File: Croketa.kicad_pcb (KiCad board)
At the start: 2 copper layers, 17.8 x 33 mm, 23 parts, among them J1 USB_B_Micro, J2 CORTEX_DEBUGPTH, P1 Digital, P3 Analog, P4 Analog, SW1 SW_DPST_x2, U1 AP2112K-3.3TRG1, U2 ATSAMD21E18A-AF

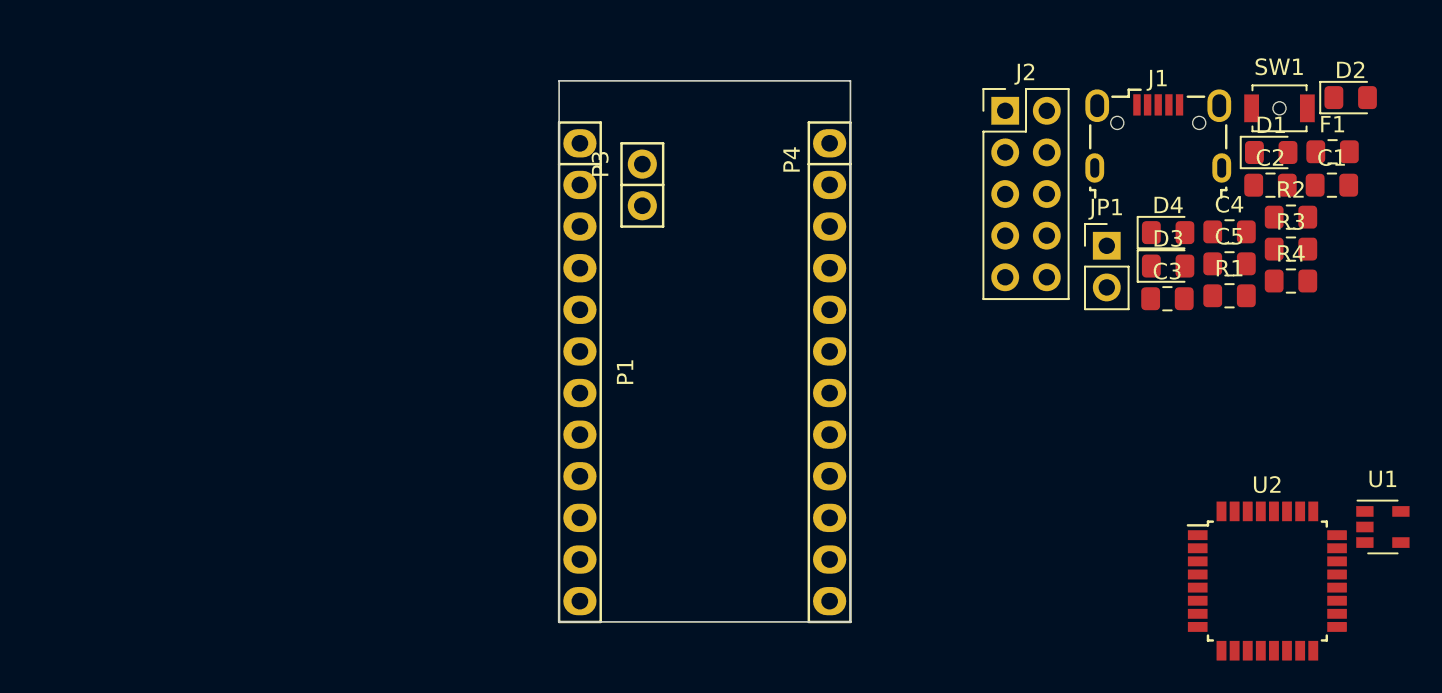
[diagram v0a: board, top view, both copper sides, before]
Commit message: Second arrangement of components in pcb
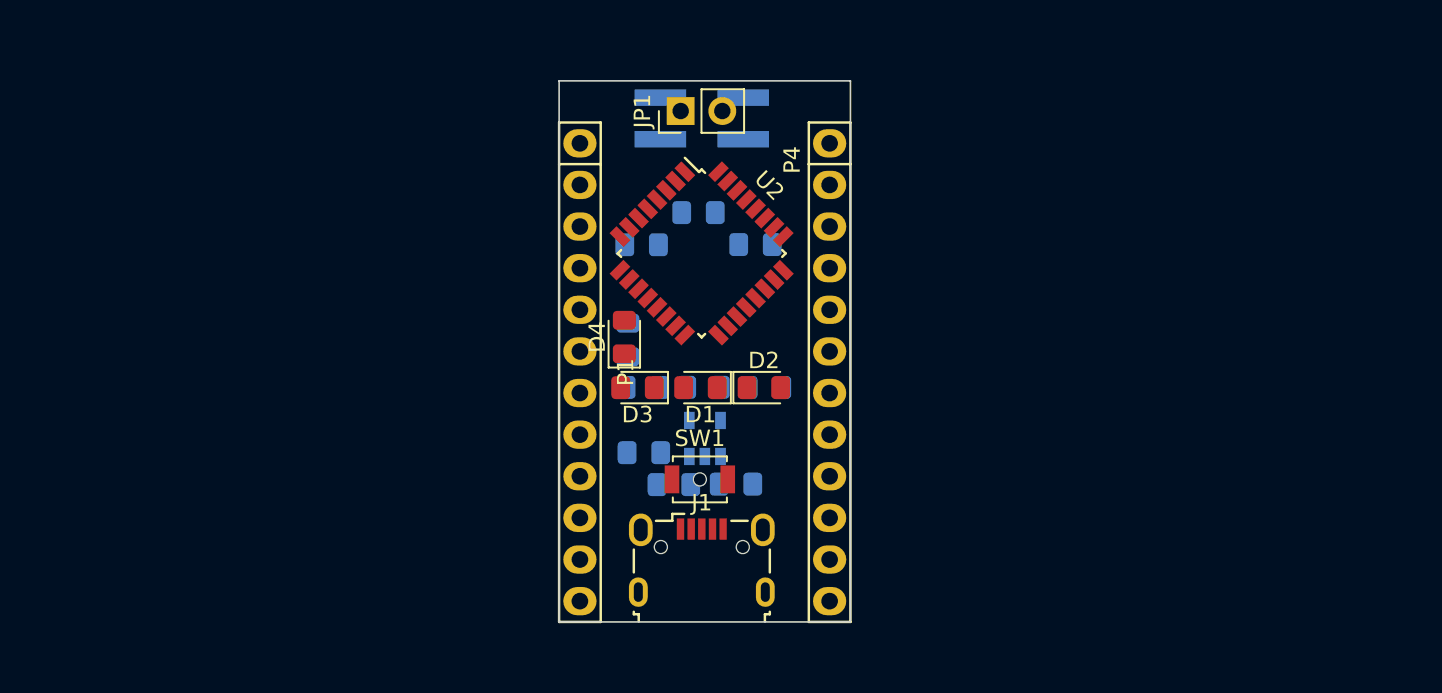
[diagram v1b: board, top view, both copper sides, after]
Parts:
- removed P3: Analog, Socket_Arduino_Pro_Mini:Socket_Strip_Arduino_1x02
- C1, C2, C3, C4, C5, F1, R1, R2, R3, R4, U1: moved to B.Cu
- J2: value CORTEX_DEBUGPTH -> Conn_02x02_Odd_Even; footprint Connector_PinHeader_2.54mm:PinHeader_2x05_P2.54mm_Vertical -> Connector_PinHeader_2.54mm:PinHeader_2x02_P2.54mm_Vertical_SMD; moved to B.Cu
- moved F1 45.9 mm to (142.3, 104.0), turned to 180 degrees
- moved C1 44.1 mm to (144.2, 105.9), turned to 180 degrees
- moved SW1 42.0 mm to (145.8, 105.6)
- moved U1 41.7 mm to (146.1, 103.1), turned to 90 degrees
- moved R4 40.6 mm to (141.4, 97.1), turned to 90 degrees
- moved R3 40.4 mm to (142.3, 100.0), turned to 180 degrees
- moved D2 40.0 mm to (149.7, 100.0)
- moved U2 39.9 mm to (145.9, 91.8), turned to 315 degrees
- moved J1 38.0 mm to (145.9, 110.5)
- moved D1 37.7 mm to (145.8, 100.0), turned to 180 degrees
- moved C2 37.4 mm to (148.0, 105.9), turned to 180 degrees
- moved D4 33.8 mm to (141.1, 96.9), turned to 90 degrees
- moved R2 33.7 mm to (149.7, 100.0)
- moved D3 33.2 mm to (141.9, 100.0), turned to 180 degrees
- moved R1 32.6 mm to (146.0, 100.0), turned to 180 degrees
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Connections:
- J2 pad 2: /SWDIO -> GND
- J2 pad 3: GND -> /SWDIO
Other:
- net class Default: clearance 0.2 -> 0.25; trace_width 0.25 -> 0.3; via_dia 0.6 -> 0.8; via_drill 0.4 -> 0.5
- rule trace_clearance: 0.2 -> 0.25

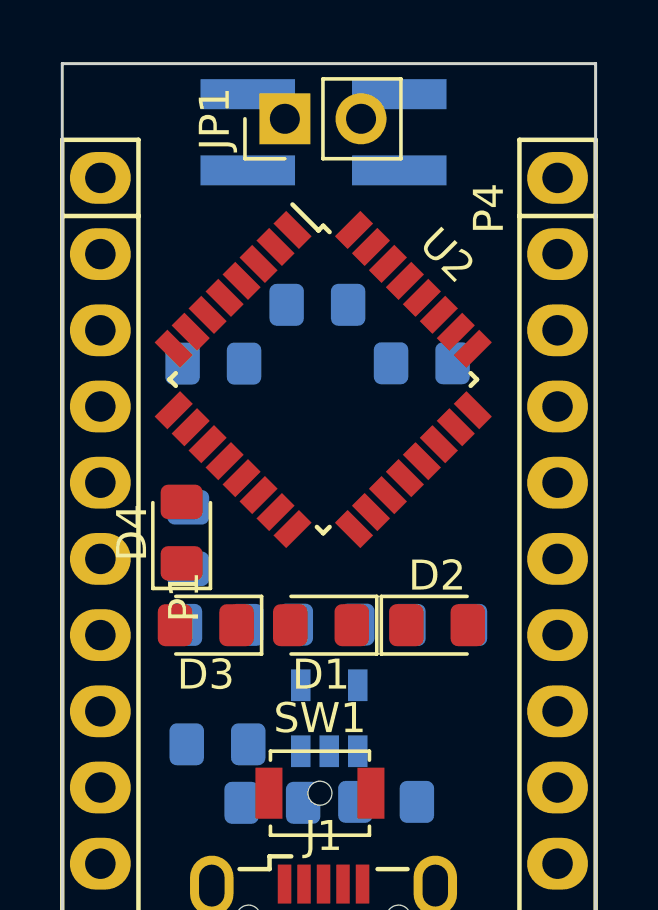
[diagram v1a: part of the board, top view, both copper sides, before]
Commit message: Add logos
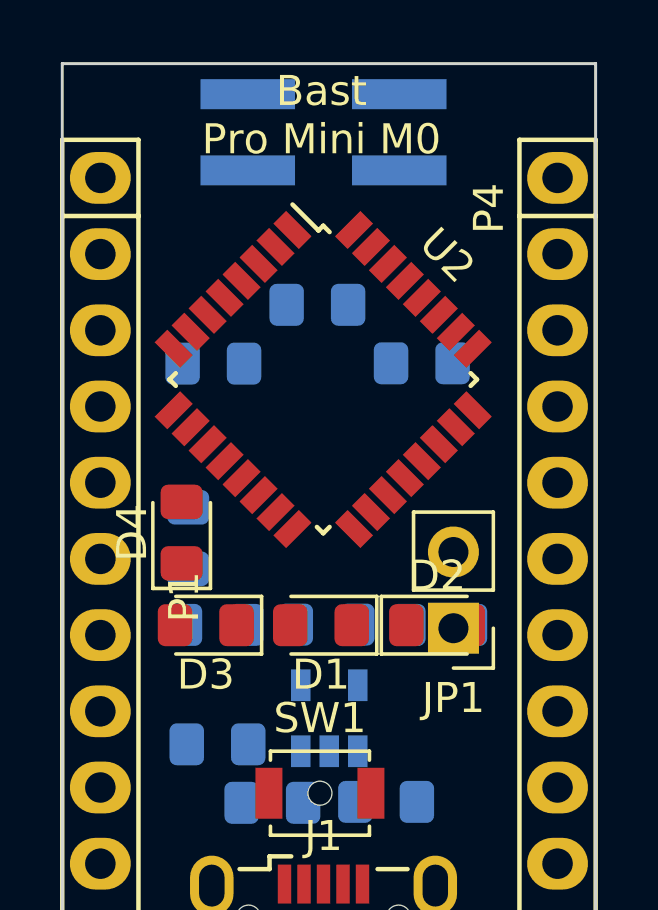
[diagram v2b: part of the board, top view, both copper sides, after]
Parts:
- added G***: LOGO, Aesthetics:electronic_cats_logo_4x3, B.Cu at (148.0, 94.9)
- added REF***: OSHW-Logo_5.7x6mm_SilkScreen, Symbols:OSHW-Logo_5.7x6mm_SilkScreen, B.Cu at (145.8, 111.1)
- moved JP1 17.9 mm to (150.2, 100.1), turned to 180 degrees
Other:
- board text added: "Bast Pro Mini M0"

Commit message: Pre router
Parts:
- removed D2, D3: LED, LED_SMD:LED_0805_2012Metric_Pad1.15x1.40mm_HandSolder
- added G***: LOGO, LOGO, F.Cu at (160.9, 104.7)
- added G***: LOGO, LOGO, F.Cu at (162.8, 90.8)
- moved J2 28.2 mm to (146.0, 111.8)
- moved J1 26.0 mm to (146.1, 84.5), turned to 180 degrees
- moved U2 11.3 mm to (146.1, 103.1)
- moved D4 10.8 mm to (149.6, 90.2)
- moved D1 9.78 mm to (147.2, 90.3), turned to 270 degrees
- moved SW1 6.65 mm to (145.6, 112.2)
- moved JP1 3.30 mm to (150.3, 96.8)

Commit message: Dimensions of Bast Pro Mini M0
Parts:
- C3, C4, C5: moved to F.Cu
- D1: value LED -> POWER
- moved G*** 8.79 mm to (168.8, 100.8)
- moved C4 7.25 mm to (142.2, 93.3)
- moved C5 3.51 mm to (142.2, 89.2), turned to 0 degrees
- moved SW1 1.88 mm to (144.9, 110.5)
- moved U2 1.17 mm to (145.3, 102.2)
- moved D1 0.50 mm to (147.2, 89.8), turned to 90 degrees
- moved D4 0.45 mm to (149.6, 89.7)
- moved JP1 0.20 mm to (150.3, 96.6)
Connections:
- net /AREF renamed Net-(U2-Pad4)
- C1 pad 1: +5V -> VCC
- F1 pad 1: +5V -> VCC
- J1 pad 2: Net-(J1-Pad2) -> /D-
- J1 pad 3: Net-(J1-Pad3) -> /D+
- P1 pad 3: /Reset -> /RESET
- R2 pad 2: /TX_LED -> /LED
- SW1 pad 1: /Reset -> /RESET
- U1 pad 1: +5V -> VCC
- U1 pad 3: +5V -> VCC
- U2 pad 11: /4 -> /SDA
- U2 pad 12: /3(**) -> /SCL
- U2 pad 14: /A4 -> /LED
- U2 pad 21: /SDA -> /4
- U2 pad 22: /SCL -> /3(**)
- U2 pad 23: /USB_D- -> /D-
- U2 pad 24: /USB_D+ -> /D+
- U2 pad 25: /TX_LED -> /6(**)
- U2 pad 27: /USB_HOST_EN -> /7

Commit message: Add art
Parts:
- removed the G*** at (168.8, 100.8)
- removed the G*** at (162.8, 90.8)
- added G***: LOGO, LOGO, F.Cu at (143.5, 112.1)
- added G***: LOGO, LOGO, F.Cu at (145.2, 93.8)
- added G***: LOGO, LOGO, F.Cu at (149.6, 110.3)
- moved REF*** 23.0 mm to (146.1, 88.1)
- moved G*** 2.05 mm to (145.9, 95.0)

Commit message: New pcb's Bast
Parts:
- removed D4: LED, LED_SMD:LED_0805_2012Metric_Pad1.15x1.40mm_HandSolder
- removed R3, R4: 330, Resistor_SMD:R_0805_2012Metric_Pad1.15x1.40mm_HandSolder
- added D2: LED, LED_SMD:LED_0805_2012Metric_Pad1.15x1.40mm_HandSolder, F.Cu at (142.9, 89.8)
- C1, C2, C3, C4, C5: footprint Capacitor_SMD:C_0805_2012Metric_Pad1.15x1.40mm_HandSolder -> Capacitor_SMD:C_0603_1608Metric_Pad1.05x0.95mm_HandSolder
- P2: renamed from JP1; value Jumper_NC_Small -> ADC
- R1, R2: footprint Resistor_SMD:R_0805_2012Metric_Pad1.15x1.40mm_HandSolder -> Resistor_SMD:R_0603_1608Metric_Pad1.05x0.95mm_HandSolder; moved to F.Cu
- moved G*** 52.2 mm to (94.0, 90.1)
- moved REF*** 51.4 mm to (94.8, 84.2)
- moved G*** 36.2 mm to (108.3, 103.4)
- moved G*** 36.0 mm to (111.2, 81.7)
- moved G*** 34.4 mm to (115.3, 107.5)
- moved C5 21.4 mm to (151.1, 108.7), turned to 270 degrees
- moved C2 17.4 mm to (141.5, 89.8), turned to 270 degrees
- moved C4 17.1 mm to (149.6, 108.7), turned to 270 degrees
- moved C1 16.4 mm to (147.7, 89.9), turned to 90 degrees
- moved F1 15.9 mm to (149.6, 89.8), turned to 90 degrees
- moved U1 13.4 mm to (144.7, 89.8), turned to 180 degrees
- moved R2 13.4 mm to (141.2, 89.7), turned to 270 degrees
- moved R1 11.1 mm to (150.2, 89.7), turned to 270 degrees
- moved C3 5.45 mm to (145.4, 95.7), turned to 180 degrees
- moved D1 1.25 mm to (148.4, 89.9), turned to 270 degrees
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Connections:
- P2 pad 1: Net-(JP1-Pad1) -> /SDA
- P2 pad 2: GND -> /SCL
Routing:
- net GND: track 0.00 -> 62.8 mm, vias 0 -> 3
- net /1(Tx): track 0.00 -> 34.9 mm, vias 0 -> 1
- net /0(Rx): track 0.00 -> 34.0 mm, vias 0 -> 1
- net /D+: track 0.00 -> 28.0 mm, vias 0 -> 2
- net /D-: track 0.00 -> 27.3 mm, vias 0 -> 2
- net /11(**/MOSI): track 0.00 -> 24.8 mm, vias 0 -> 1
- net /8: track 0.00 -> 23.7 mm, vias 0 -> 1
- net /10(**/SS): track 0.00 -> 21.0 mm, vias 0 -> 2
- net +3V3: track 0.00 -> 20.8 mm, vias 0 -> 3
- net /9(**): track 0.00 -> 20.7 mm, vias 0 -> 1
- net /A3: track 0.00 -> 20.4 mm
- net /7: track 0.00 -> 17.3 mm
- net /13(SCK): track 0.00 -> 15.4 mm, vias 0 -> 1
- net /12(MISO): track 0.00 -> 13.8 mm, vias 0 -> 1
- net /SCL: track 0.00 -> 12.7 mm
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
